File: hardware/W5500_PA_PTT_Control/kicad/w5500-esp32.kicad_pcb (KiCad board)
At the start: 4 copper layers, 72 x 115 mm, 26 parts, among them J1 ESP32_DevKitC_Socket_40P_25.4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, J2 DC_IN_13V8, J5 Power, J6 PTT_ON, Q1 2SC1815, Q3 2SC1815, Q5 2SJ334, U1 TA48033S, U2 L7805

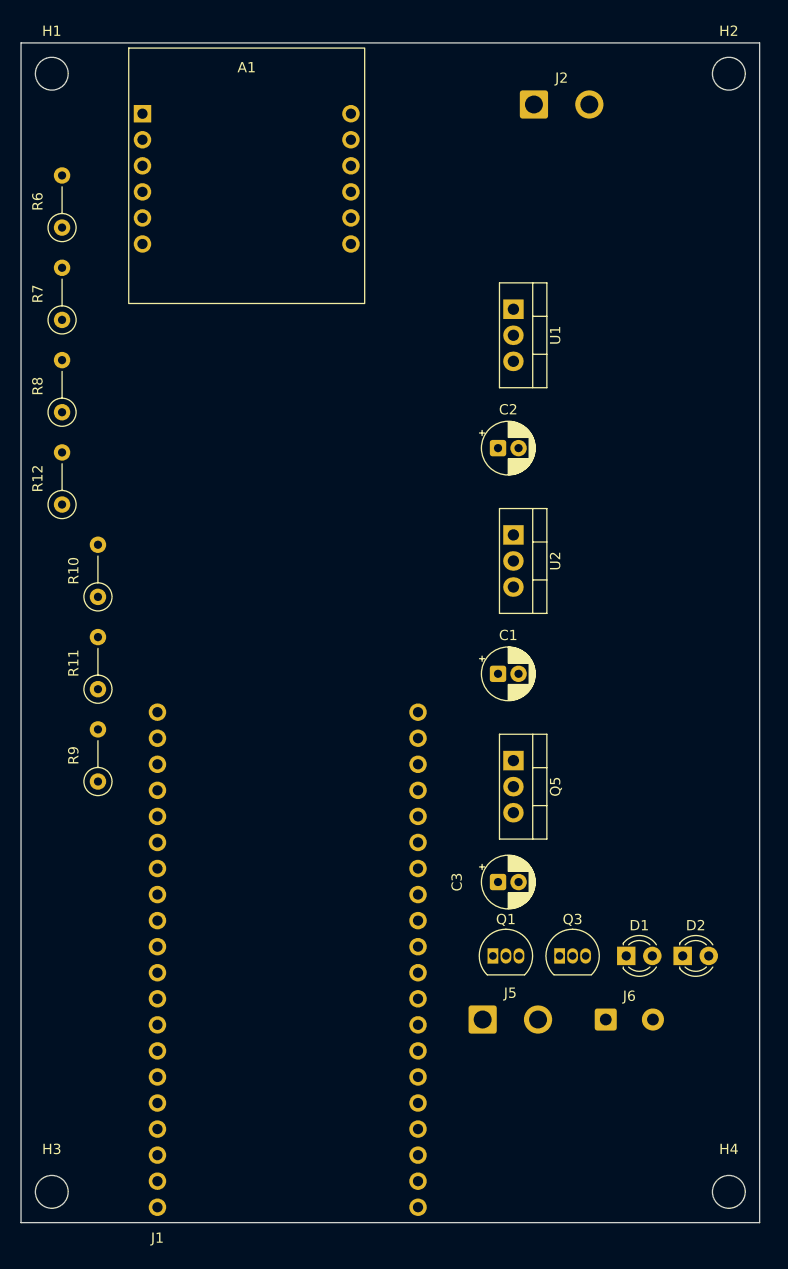
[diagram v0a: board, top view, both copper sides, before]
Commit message: W5500制御基板: 自動配線・12V系統強化・外付けLED/XHコネクタ化と総点検の修正
- 回路図のGND記号の値が空で別ネットになっていたのを修正
- 内層をGND・+12Vの全面ベタにし、12V出力(/Power)を表裏4mmで配線、残りをFreeroutingで自動配線
- Q1/Q3を2.54mmピッチのTO-92に、R8を1/2W抵抗用フットプリントに変更
- D1/D2を外付けにしてJ7/J8で接続、J6/J7/J8をJST XH(B2B-XH-A)に変更
- C2をTA48033Sデータシートどおり33µF、C1/C3を0.33µFに変更
- Q3ベースにプルダウンR13(10k)を追加、J1のGNDピン21〜24・40を接続
- 仕様書・接続一覧(日英)を更新しWord/PDF・回路図PDF/SVGを再生成

Co-Authored-By: Claude Opus 5.5 <noreply@anthropic.com>
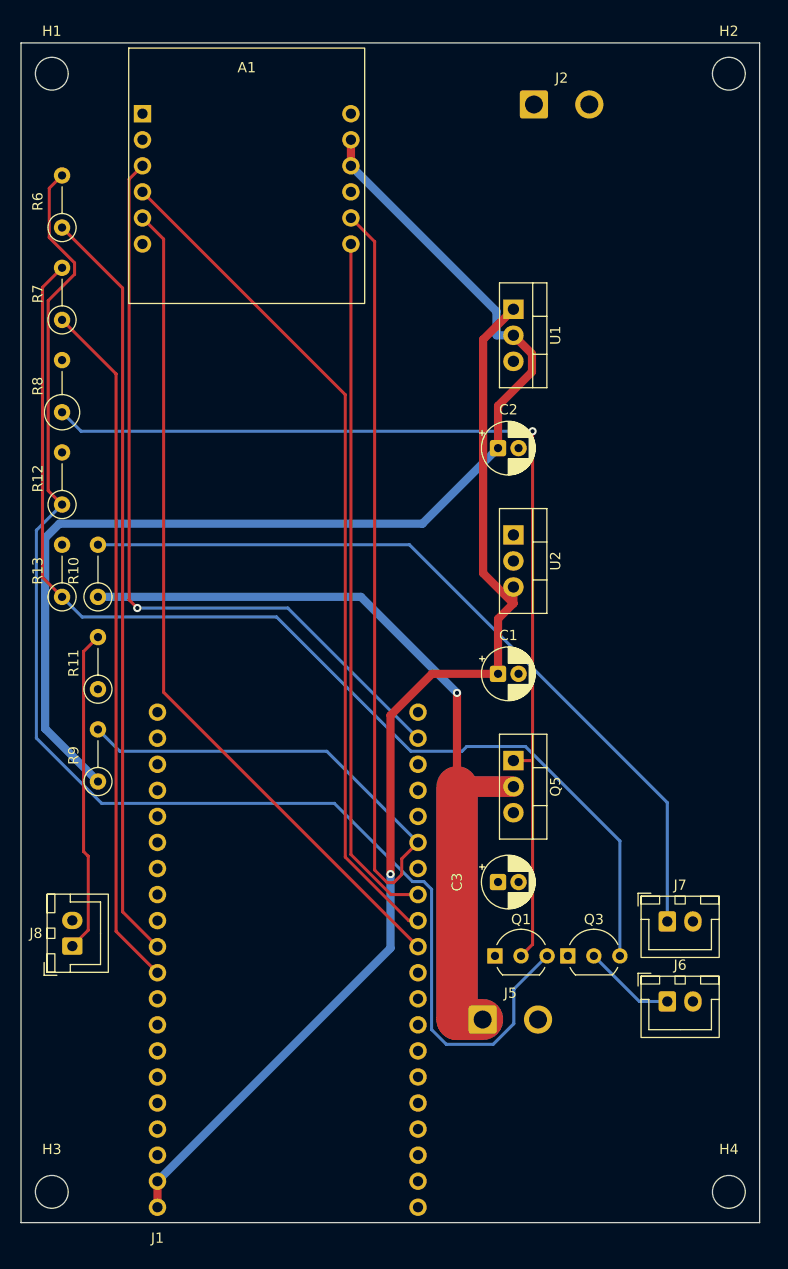
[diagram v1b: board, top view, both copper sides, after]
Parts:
- removed D1: LED_Red_3mm, LED_THT:LED_D3.0mm
- removed D2: LED_Green_3mm, LED_THT:LED_D3.0mm
- added J7: LED_PWR, Connector_JST:JST_XH_B2B-XH-A_1x02_P2.50mm_Vertical, F.Cu at (127.0, 132.1)
- added J8: LED_12V, Connector_JST:JST_XH_B2B-XH-A_1x02_P2.50mm_Vertical, F.Cu at (69.0, 134.5)
- added R13: 10k, Resistor_THT:R_Axial_DIN0207_L6.3mm_D2.5mm_P5.08mm_Vertical, F.Cu at (68.0, 100.5)
- C1, C3: value 0.1uF -> 0.33uF
- C2: value 0.1uF -> 33uF
- J6: footprint Connector_Wire:SolderWire-0.5sqmm_1x02_P4.6mm_D0.9mm_OD2.1mm -> Connector_JST:JST_XH_B2B-XH-A_1x02_P2.50mm_Vertical
- Q1, Q3: footprint Package_TO_SOT_THT:TO-92_Inline -> Package_TO_SOT_THT:TO-92_Inline_Wide
- R8: footprint Resistor_THT:R_Axial_DIN0207_L6.3mm_D2.5mm_P5.08mm_Vertical -> Resistor_THT:R_Axial_DIN0309_L9.0mm_D3.2mm_P5.08mm_Vertical
- moved J6 6.25 mm to (127.0, 139.9)
- moved Q3 0.80 mm to (117.3, 135.5)
- moved Q1 0.20 mm to (110.2, 135.5)
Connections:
- J1 pad 21: unconnected-(J1-GND-Pad21) -> GND
- J1 pad 22: unconnected-(J1-GND-Pad22) -> GND
- J1 pad 23: unconnected-(J1-GND-Pad23) -> GND
- J1 pad 24: unconnected-(J1-GND-Pad24) -> GND
- J1 pad 40: unconnected-(J1-GND-Pad40) -> GND
- J1 pad 7: <NO NET> -> GND
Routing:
- net Net-(Q1-B): track 0.00 -> 134.8 mm
- net /+3V3_A: track 0.00 -> 113.4 mm
- net /+5v0: track 0.00 -> 109.7 mm, vias 0 -> 1
- net Net-(Q3-B): track 0.00 -> 109.5 mm
- net /Power: track 0.00 -> 109.4 mm, vias 0 -> 1
- net /GPIO21_W5500_RST: track 0.00 -> 107.6 mm
- net Net-(Q1-C): track 0.00 -> 100.1 mm, vias 0 -> 1
- net Net-(A1-SCK): track 0.00 -> 82.7 mm
- net Net-(A1-CS): track 0.00 -> 82.2 mm
- net Net-(J7-Pin_1): track 0.00 -> 77.5 mm
- net Net-(A1-MOSI): track 0.00 -> 76.6 mm, vias 0 -> 1
- net /GPIO26_PA: track 0.00 -> 74.0 mm
- net Net-(A1-MISO): track 0.00 -> 67.7 mm
- net /GPIO27_PTT: track 0.00 -> 67.5 mm
- net Net-(J8-Pin_1): track 0.00 -> 31.5 mm
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- added copper zone on In2.Cu, net +12V
- added copper zone on In1.Cu, net GND

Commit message: W5500制御基板: JLCPCB発注データ・実装図を追加、J6/J7を放熱器から離す
- fabrication/jlcpcb: ガーバー・ドリル(ZIP)、部品表、発注設定のREADMEを追加
- fabrication/assembly: 部品配置図PDFと3D実装図(放熱器・W5500・ESP32の簡易モデル付き)を追加
- シルクに端子名・基板名・注文番号位置を追加、はみ出していた部品番号を修正
- J6/J7をQ5の放熱器から5mm以上離して再配線
- 仕様書(日英)の配置説明を更新

Co-Authored-By: Claude Opus 5.5 <noreply@anthropic.com>
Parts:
- moved J6 4.90 mm to (127.0, 144.8)
- moved J7 4.90 mm to (127.0, 137.0)
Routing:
- net Net-(J7-Pin_1): track 77.5 -> 82.4 mm
- net /PTT_ON: track 9.00 -> 12.3 mm
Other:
- board text added: "+12V"
- board text added: "12V OUT"
- board text added: "1:PTT 2:GND"
- board text added: "GND"
- board text added: "JLCJLCJLCJLC"
- board text added: "W5500 PA/PTT Control Rev.2.6"

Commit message: W5500制御基板: J6/J7をW5500とESP32の間へ移動、シルクに設計者名を追加
- J7(左)・J6(右)をW5500モジュールとESP32ソケットの間に横並びで配置し再配線
- シルクに「designed by JA6FUF/JH1XHX」を追加
- 仕様書(日英)の配置説明、JLCPCB発注データ(ガーバーZIP・README)、実装図を更新

Co-Authored-By: Claude Opus 5.5 <noreply@anthropic.com>
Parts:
- moved J7 67.9 mm to (80.0, 88.0)
- moved J6 66.7 mm to (92.0, 88.0)
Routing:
- net Net-(J7-Pin_1): track 82.4 -> 11.6 mm
- net /PTT_ON: track 12.3 -> 59.3 mm, vias 0 -> 1
- net Net-(Q3-B): track 109.5 -> 129.3 mm
- net Net-(Q1-B): track 134.8 -> 116.4 mm, vias 0 -> 1
- net Net-(A1-MOSI): track 76.6 -> 66.9 mm
- net /+3V3_A: track 113.4 -> 105.3 mm
- net /GPIO21_W5500_RST: track 107.6 -> 106.9 mm
- net /Power: track 109.4 -> 108.8 mm
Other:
- board text added: "designed by JA6FUF/JH1XHX"

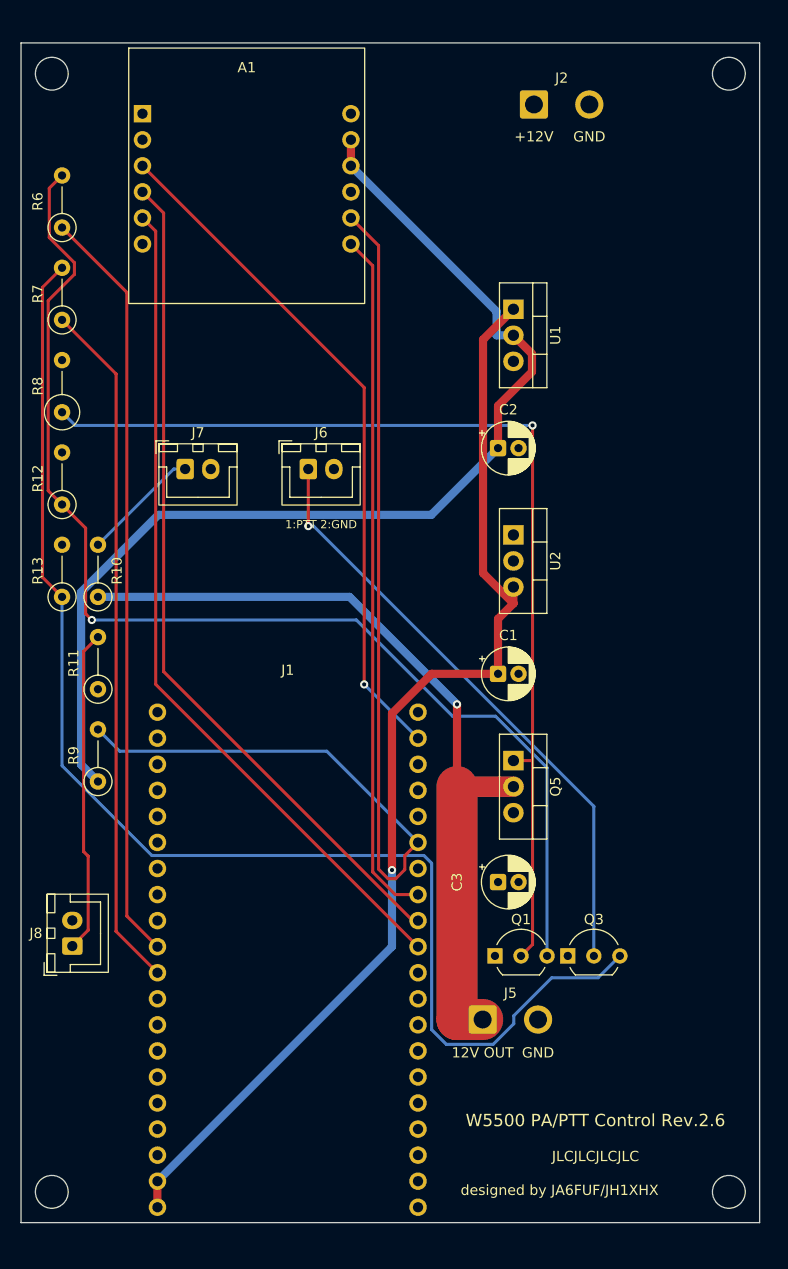
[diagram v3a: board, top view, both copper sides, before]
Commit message: W5500制御基板: +5Vを信号線から離し、J1のピン間に配線を通さないよう再配線、J1の12番ピンを未接続に
- J1の35番ピン(W5500 RST)の配線が+5Vのビアに0.3mmまで近づいていたため、+5V(/+5v0)を
  ネットクラスSupply5V(間隔0.5mm、線幅0.6mm)に分けて再配線した。C1自身の足の間(0.4mm)だけは
  w5500-esp32.kicad_druの例外ルールで0.25mmとする。
- はんだブリッジを避けるため、J1のピンとピンの間に表裏とも配線禁止領域を置いた
  (同じ+5Vの1番・2番の間を除く)。ピン間を突き抜ける配線は0本。
- 回路図でJ1の12番ピン(GPIO25)を未接続(×)にし、MCU1に残っていたGPIO25_LNAラベルを削除した。
- DRC違反0・未配線0。ガーバー・ドリル(スルーホール103穴、ビア4)、回路図PDF/SVG、仕様書・接続一覧を更新した。

Co-Authored-By: Claude Opus 5.5 <noreply@anthropic.com>
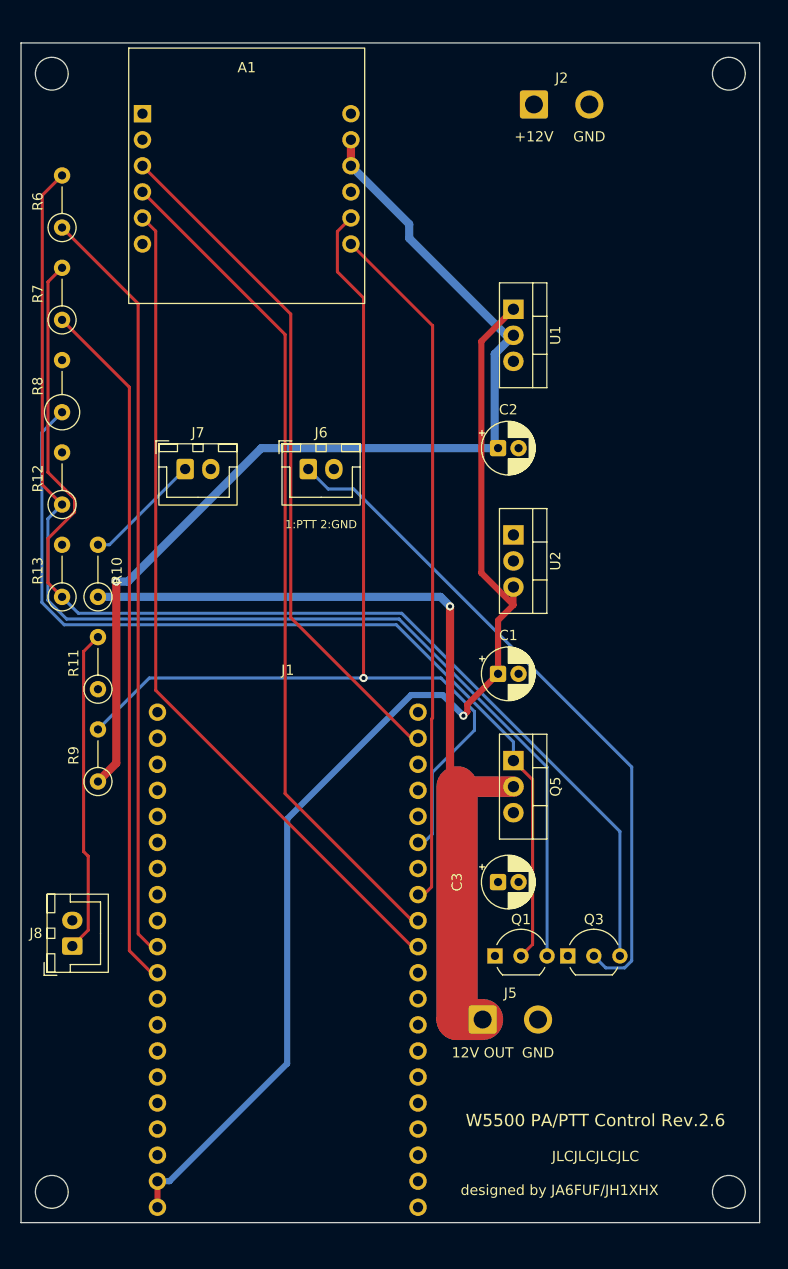
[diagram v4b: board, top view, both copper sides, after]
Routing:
- net Net-(Q3-B): track 129.3 -> 111.4 mm
- net /PTT_ON: track 59.3 -> 66.9 mm, vias 1 -> 0
- net Net-(Q1-C): track 100.4 -> 93.1 mm, vias 1 -> 0
- net /Power: track 108.8 -> 114.0 mm
- net /GPIO21_W5500_RST: track 106.9 -> 102.0 mm, vias 0 -> 1
- net /+3V3_A: track 105.3 -> 100.6 mm, vias 0 -> 1
- net /+5v0: track 109.8 -> 112.8 mm
- net Net-(Q1-B): track 116.4 -> 117.4 mm, vias 1 -> 0
- net Net-(A1-MOSI): track 66.9 -> 67.3 mm, vias 1 -> 0

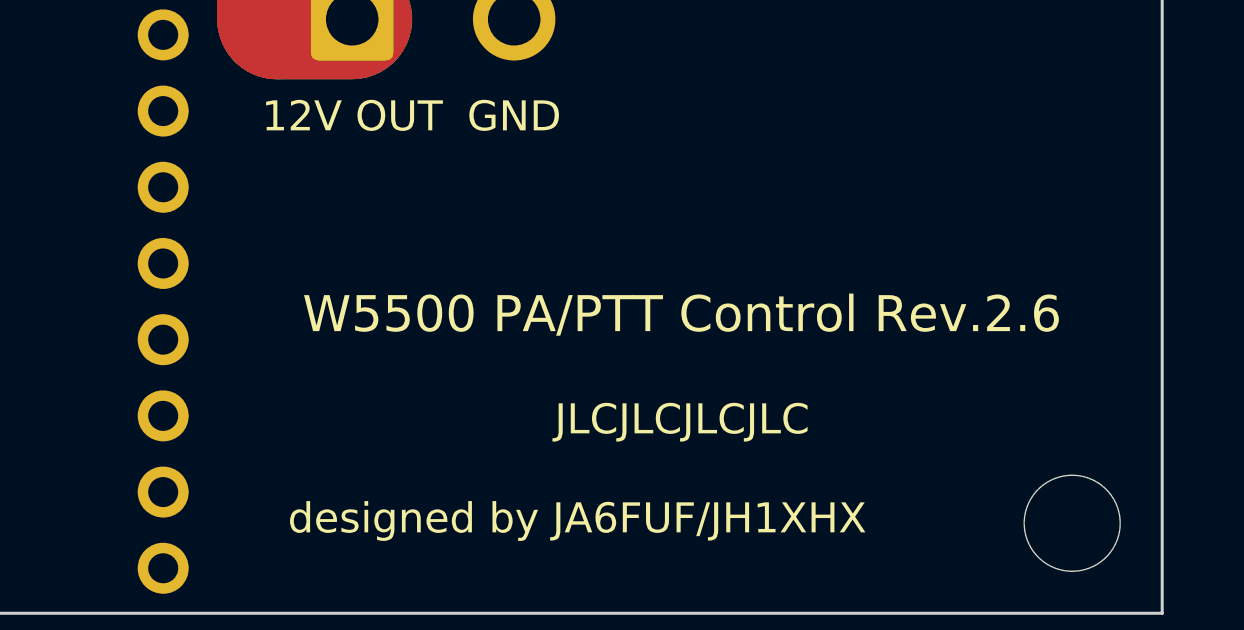
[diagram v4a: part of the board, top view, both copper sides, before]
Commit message: W5500制御基板: シルクの版数をRev.1.0にし、仕様書との版数の対応表を追加
- 基板のシルクを「W5500 PA/PTT Control Rev.2.6」から「Rev.1.0」に変更(最初に製造する基板)。
  ガーバーは表面シルクのみ更新。
- 仕様書の版数(Rev.2.6)と基板の版数は別番号で管理し、仕様書冒頭に「版数の対応表」を追加
  (仕様書Rev.2.6=基板Rev.1.0)。README・発注用READMEの版数表記も更新。

Co-Authored-By: Claude Opus 5.5 <noreply@anthropic.com>
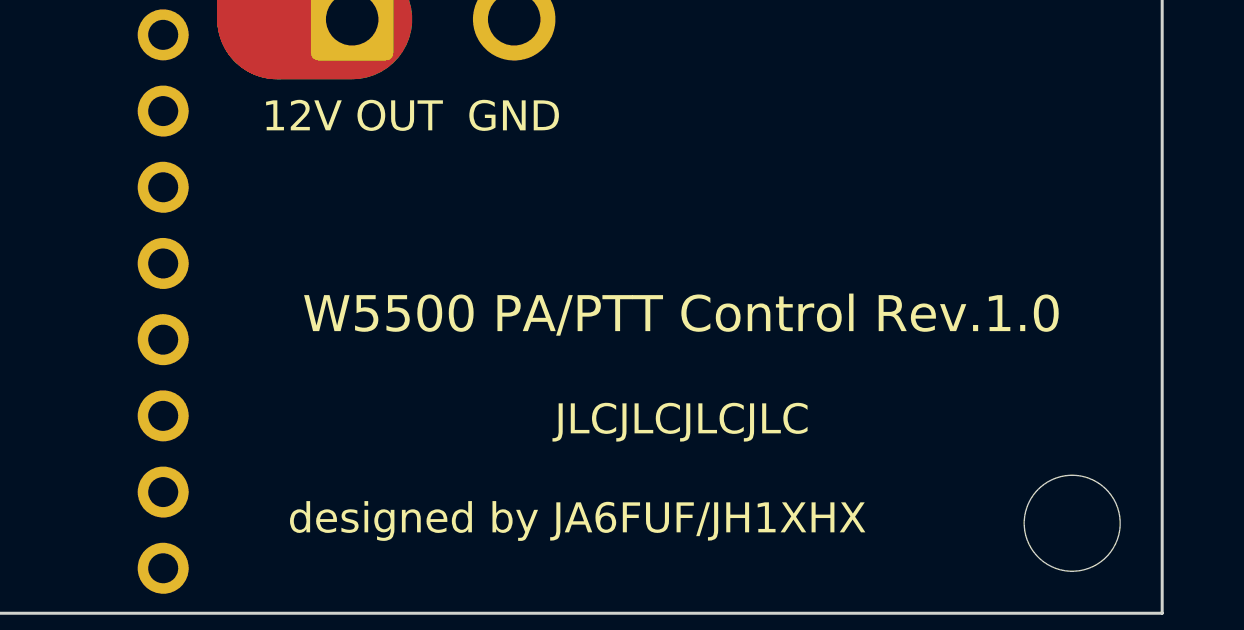
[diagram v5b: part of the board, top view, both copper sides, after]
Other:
- board text added: "W5500 PA/PTT Control Rev.1.0"
- board text removed: "W5500 PA/PTT Control Rev.2.6"
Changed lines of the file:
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@@
 		)
 	)
-	(gr_text "W5500 PA/PTT Control Rev.2.6"
+	(gr_text "W5500 PA/PTT Control Rev.1.0"
 		(at 120 151.5 0)
 		(layer "F.SilkS")

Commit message: W5500制御基板 Rev.1.1: 放熱器の取付ピン用のめっき無し穴を追加
- 秋月105054(GEC 20PB020)のピン(φ1.4mm、間隔12.5mm、取付面から3.5mm奥)用にφ1.8mmのめっき無し穴をU1・U2・Q5の放熱器ごとに2個(HS1〜HS3)
- 金属ピンが内層のGND・+12Vベタや配線とショートしないよう、穴の縁から1mm以内は全層で銅箔なし
- 穴にかかっていたPTT_ONの配線を移動。DRC違反0・未接続0
- M3穴の高さを基板から19mmに訂正(仕様書・基板の注記)
- シルクの版数をRev.1.1、仕様書をRev.2.7にし、版数の対応表に追記
- ガーバー・ドリル・ZIPとREADMEを更新

Co-Authored-By: Claude Opus 5.5 <noreply@anthropic.com>
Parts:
- added HS1: Heatsink_20PB020, project_footprints:Heatsink_GEC_20PB020_Pins_P12.5mm, F.Cu at (118.7, 75.0)
- added HS2: Heatsink_20PB020, project_footprints:Heatsink_GEC_20PB020_Pins_P12.5mm, F.Cu at (118.7, 97.0)
- added HS3: Heatsink_20PB020, project_footprints:Heatsink_GEC_20PB020_Pins_P12.5mm, F.Cu at (118.7, 119.0)
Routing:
- net /PTT_ON: track 66.9 -> 68.7 mm
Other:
- board text added: "W5500 PA/PTT Control Rev.1.1"
- board text added: "放熱器 Q5 20x20 (M3穴 高さ19)"
- board text added: "放熱器 U1 20x20 (M3穴 高さ19)"
- board text added: "放熱器 U2 20x20 (M3穴 高さ19)"
- board text removed: "W5500 PA/PTT Control Rev.1.0"
- board text removed: "放熱器 Q5 20x20 (M3穴 高さ18)"
- board text removed: "放熱器 U1 20x20 (M3穴 高さ18)"
- board text removed: "放熱器 U2 20x20 (M3穴 高さ18)"

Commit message: W5500制御基板: 基板ファイルのW5500/ESP32/放熱器に3Dモデルを割り当て、放熱器の値を105054に
ライブラリ側にだけ入っていた3Dモデル指定を基板(A1/J1/HS1-3)にも反映。
ガーバー・穴データは変化なし(提出済みZIPと同一)。

Co-Authored-By: Claude Opus 5.5 <noreply@anthropic.com>
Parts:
- HS1, HS2, HS3: value Heatsink_20PB020 -> 105054
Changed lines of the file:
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@@
 		)
 		(embedded_fonts no)
+		(model "${KIPRJMOD}/3dmodels/W5500_Lite_USR-ES1.wrl"
+			(offset
+				(xyz 0 0 0)
+			)
+			(scale
+				(xyz 1 1 1)
+			)
+			(rotate
+				(xyz 0 0 0)
+			)
+		)
 	)
 	(footprint "Capacitor_THT:CP_Radial_D5.0mm_P2.00mm"
@@
 			)
 		)
-		(property "Value" "Heatsink_20PB020"
-			(at 0 11 0)
+		(property "Value" "105054"
+			(at 6.5 0 0)
 			(layer "F.Fab")
-			(hide yes)
 			(effects
 				(font
@@
 		)
 		(embedded_fonts no)
+		(model "${KIPRJMOD}/3dmodels/Heatsink_GEC_20PB020.wrl"
+			(offset
+				(xyz 0 0 0)
+			)
+			(scale
+				(xyz 1 1 1)
+			)
+			(rotate
+				(xyz 0 0 0)
+			)
+		)
 	)
 	(footprint "project_footprints:Socket_2x20_P2.54mm_25.4mm_DevKitC"
@@
 		)
 		(embedded_fonts no)
+		(model "${KIPRJMOD}/3dmodels/Freenove_ESP32_WROOM.wrl"
+			(offset
+				(xyz 0 0 0)
+			)
+			(scale
+				(xyz 1 1 1)
+			)
+			(rotate
+				(xyz 0 0 0)
+			)
+		)
 	)
 	(footprint "Package_TO_SOT_THT:TO-92_Inline_Wide"
@@
 			)
 		)
-		(property "Value" "Heatsink_20PB020"
-			(at 0 11 0)
+		(property "Value" "105054"
+			(at 6.5 0 0)
 			(layer "F.Fab")
-			(hide yes)
 			(effects
 				(font
@@
 		)
 		(embedded_fonts no)
+		(model "${KIPRJMOD}/3dmodels/Heatsink_GEC_20PB020.wrl"
+			(offset
+				(xyz 0 0 0)
+			)
+			(scale
+				(xyz 1 1 1)
+			)
+			(rotate
+				(xyz 0 0 0)
+			)
+		)
 	)
 	(footprint "project_footprints:Heatsink_GEC_20PB020_Pins_P12.5mm"
@@
 			)
 		)
-		(property "Value" "Heatsink_20PB020"
-			(at 0 11 0)
+		(property "Value" "105054"
+			(at 6.5 0 0)
 			(layer "F.Fab")
-			(hide yes)
 			(effects
 				(font
@@
 		)
 		(embedded_fonts no)
+		(model "${KIPRJMOD}/3dmodels/Heatsink_GEC_20PB020.wrl"
+			(offset
+				(xyz 0 0 0)
+			)
+			(scale
+				(xyz 1 1 1)
+			)
+			(rotate
+				(xyz 0 0 0)
+			)
+		)
 	)
 	(footprint "Resistor_THT:R_Axial_DIN0207_L6.3mm_D2.5mm_P5.08mm_Vertical"
